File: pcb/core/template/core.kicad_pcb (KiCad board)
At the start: 2 copper layers, 79.3 x 78.9 mm, 5 parts, among them J1 Conn_01x11, J2 Conn_01x11, U1 Helios

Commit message: added 3x3 core
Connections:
- net underglow-rgb renamed rgb
- J1 pad 1: perkey-rgb -> GND
- U1 pad 1: perkey-rgb -> unconnected-(U1-P0-Pad1)
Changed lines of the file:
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@@
 	(net 0 "")
 	(net 1 "col5")
-	(net 2 "perkey-rgb")
+	(net 2 "rgb")
 	(net 3 "row2")
 	(net 4 "row0")
@@
 	(net 20 "col11")
 	(net 21 "VCC")
-	(net 22 "underglow-rgb")
+	(net 22 "unconnected-(U1-P0-Pad1)")
 	(net 23 "unconnected-(U1-P3-Pad6)")
 	(net 24 "unconnected-(U1-P21-Pad24)")
@@
 			(layers "*.Cu" "*.Mask")
 			(remove_unused_layers no)
-			(net 22 "underglow-rgb")
+			(net 2 "rgb")
 			(pinfunction "Pin_1")
 			(pintype "passive")
@@
 			(layers "*.Cu" "*.Mask")
 			(remove_unused_layers no)
-			(net 2 "perkey-rgb")
+			(net 16 "GND")
 			(pinfunction "Pin_1")
 			(pintype "passive")
@@
 			(layers "*.Cu" "F.Mask")
 			(remove_unused_layers no)
-			(net 2 "perkey-rgb")
+			(net 22 "unconnected-(U1-P0-Pad1)")
 			(pinfunction "P0")
 			(pintype "bidirectional")
@@
 			(layers "*.Cu" "F.Mask")
 			(remove_unused_layers no)
-			(net 22 "underglow-rgb")
+			(net 2 "rgb")
 			(pinfunction "P25")
 			(pintype "bidirectional")

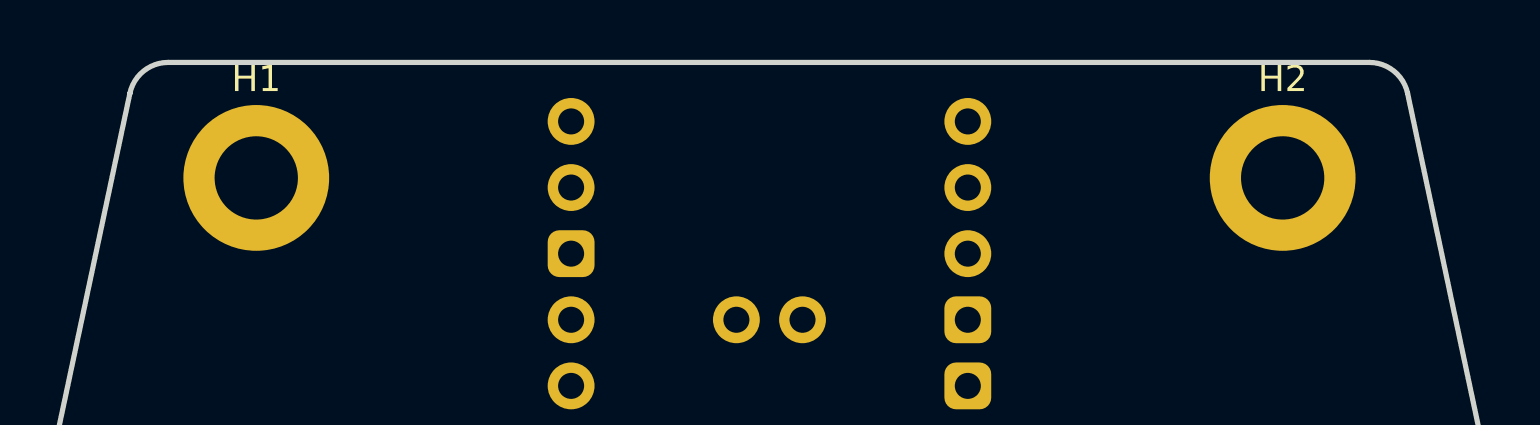
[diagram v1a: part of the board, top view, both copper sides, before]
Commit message: switched rgb back to a regular pin and 3v
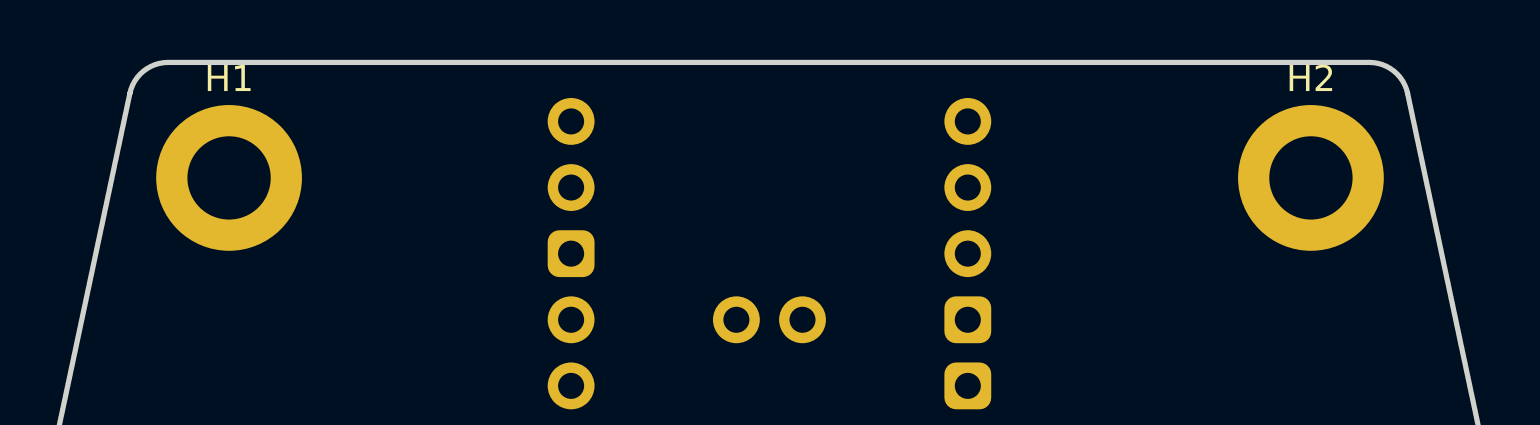
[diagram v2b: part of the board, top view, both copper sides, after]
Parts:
- moved H2 1.09 mm to (219.0, 138.9)
- moved H1 1.04 mm to (177.4, 138.9)
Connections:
- J2 pad 9: VCC -> vcc
- U1 pad 1: unconnected-(U1-P0-Pad1) -> rgb
- U1 pad 13: VCC -> unconnected-(U1-5V-Pad13)
- U1 pad 16: unconnected-(U1-3V3-Pad16) -> vcc
- U1 pad 34: rgb -> unconnected-(U1-P25-Pad34)
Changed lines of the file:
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@@
 	(net 19 "col7")
 	(net 20 "col11")
-	(net 21 "VCC")
-	(net 22 "unconnected-(U1-P0-Pad1)")
+	(net 21 "vcc")
+	(net 22 "unconnected-(U1-P25-Pad34)")
 	(net 23 "unconnected-(U1-P3-Pad6)")
 	(net 24 "unconnected-(U1-P21-Pad24)")
@@
 	(net 30 "unconnected-(U1-P23-Pad23)")
 	(net 31 "unconnected-(U1-D+-Pad32)")
-	(net 32 "unconnected-(U1-3V3-Pad16)")
+	(net 32 "unconnected-(U1-5V-Pad13)")
 	(footprint "MountingHole:MountingHole_3.2mm_M3_DIN965_Pad"
 		(layer "F.Cu")
-		(at 217.916446 138.860167)
+		(at 219.0026 138.860167)
 		(descr "Mounting Hole 3.2mm, M3, DIN965")
 		(tags "mounting hole 3.2mm m3 din965")
@@
 	(footprint "MountingHole:MountingHole_3.2mm_M3_DIN965_Pad"
 		(layer "F.Cu")
-		(at 178.485446 138.860167)
+		(at 177.4406 138.860167)
 		(descr "Mounting Hole 3.2mm, M3, DIN965")
 		(tags "mounting hole 3.2mm m3 din965")
@@
 			(layers "*.Cu" "*.Mask")
 			(remove_unused_layers no)
-			(net 21 "VCC")
+			(net 21 "vcc")
 			(pinfunction "Pin_9")
 			(pintype "passive")
@@
 			(layers "*.Cu" "F.Mask")
 			(remove_unused_layers no)
-			(net 22 "unconnected-(U1-P0-Pad1)")
+			(net 2 "rgb")
 			(pinfunction "P0")
 			(pintype "bidirectional")
@@
 			(layers "*.Cu" "F.Mask")
 			(remove_unused_layers no)
-			(net 21 "VCC")
+			(net 32 "unconnected-(U1-5V-Pad13)")
 			(pinfunction "5V")
 			(pintype "bidirectional")
@@
 			(layers "*.Cu" "F.Mask")
 			(remove_unused_layers no)
-			(net 32 "unconnected-(U1-3V3-Pad16)")
+			(net 21 "vcc")
 			(pinfunction "3V3")
 			(pintype "power_out")
@@
 			(layers "*.Cu" "F.Mask")
 			(remove_unused_layers no)
-			(net 2 "rgb")
+			(net 22 "unconnected-(U1-P25-Pad34)")
 			(pinfunction "P25")
 			(pintype "bidirectional")
@@
 	)
 	(gr_line
-		(start 173.485446 138.860167)
-		(end 178.485446 138.860167)
+		(start 172.4406 138.860167)
+		(end 177.4406 138.860167)
 		(stroke
 			(width 0.1)
@@
 	)
 	(gr_line
-		(start 222.916446 138.860167)
-		(end 217.916446 138.860167)
+		(start 223.9772 138.8618)
+		(end 219.0026 138.8618)
 		(stroke
 			(width 0.1)

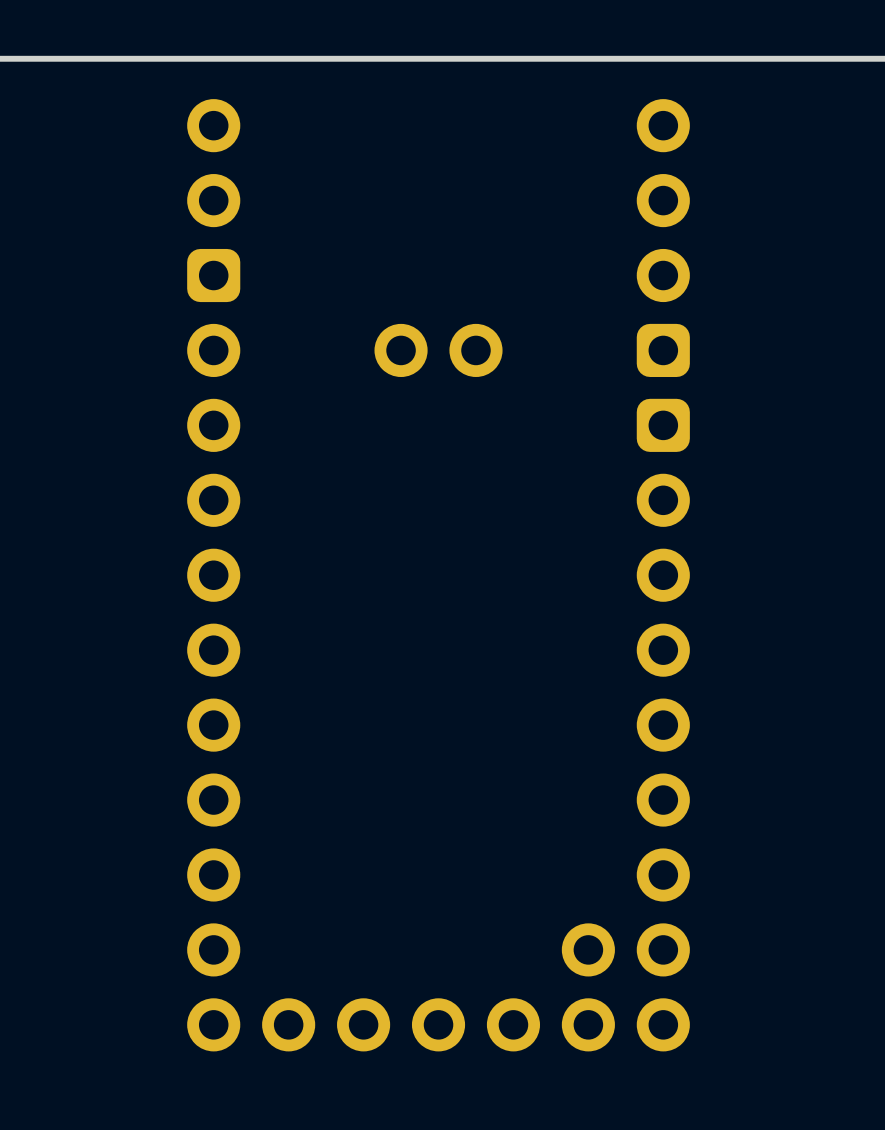
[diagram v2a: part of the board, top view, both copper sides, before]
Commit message: added jumpers for 3.3/5v rgb
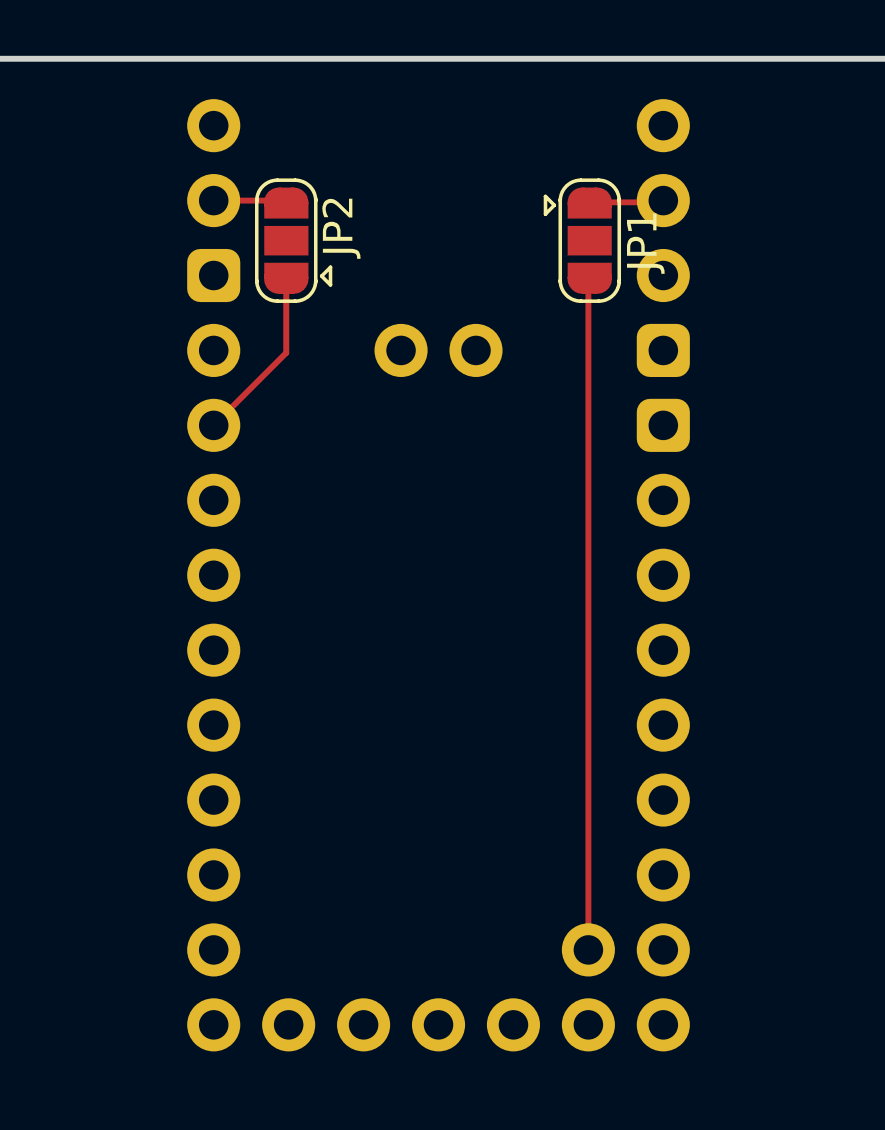
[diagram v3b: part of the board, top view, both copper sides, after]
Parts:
- added JP1: Jumper_3_Open, Jumper:SolderJumper-3_P1.3mm_Open_RoundedPad1.0x1.5mm, F.Cu at (203.3, 140.6)
- added JP2: Jumper_3_Open, Jumper:SolderJumper-3_P1.3mm_Open_RoundedPad1.0x1.5mm, F.Cu at (193.0, 140.6)
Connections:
- J2 pad 9: vcc -> vccrgb
- U1 pad 1: rgb -> Net-(JP1-A)
- U1 pad 13: unconnected-(U1-5V-Pad13) -> Net-(JP2-B)
- U1 pad 34: unconnected-(U1-P25-Pad34) -> Net-(JP1-B)
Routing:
- net Net-(JP1-B): track 0.00 -> 22.8 mm
- net vcc: track 0.00 -> 5.98 mm
- net Net-(JP1-A): track 0.00 -> 2.52 mm
- net Net-(JP2-B): track 0.00 -> 2.48 mm
